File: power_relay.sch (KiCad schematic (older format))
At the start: 35 parts, among them J18 Conn_01x03, J20 Conn_01x03, J22 Conn_01x03, J24 Conn_01x03, J26 Conn_01x03, K1 RELAY_1RT, K2 RELAY_1RT, K3 RELAY_1RT, K4 RELAY_1RT, K5 RELAY_1RT, Q1 MMBT4401-7-F, Q10 SI7113ADN-T1-GE3, Q2 MMBT4401-7-F, Q3 MMBT4401-7-F, Q4 SI7113ADN-T1-GE3, Q5 SI7113ADN-T1-GE3, Q6 SI7113ADN-T1-GE3, Q7 MMBT4401-7-F, Q8 MMBT4401-7-F, Q9 SI7113ADN-T1-GE3

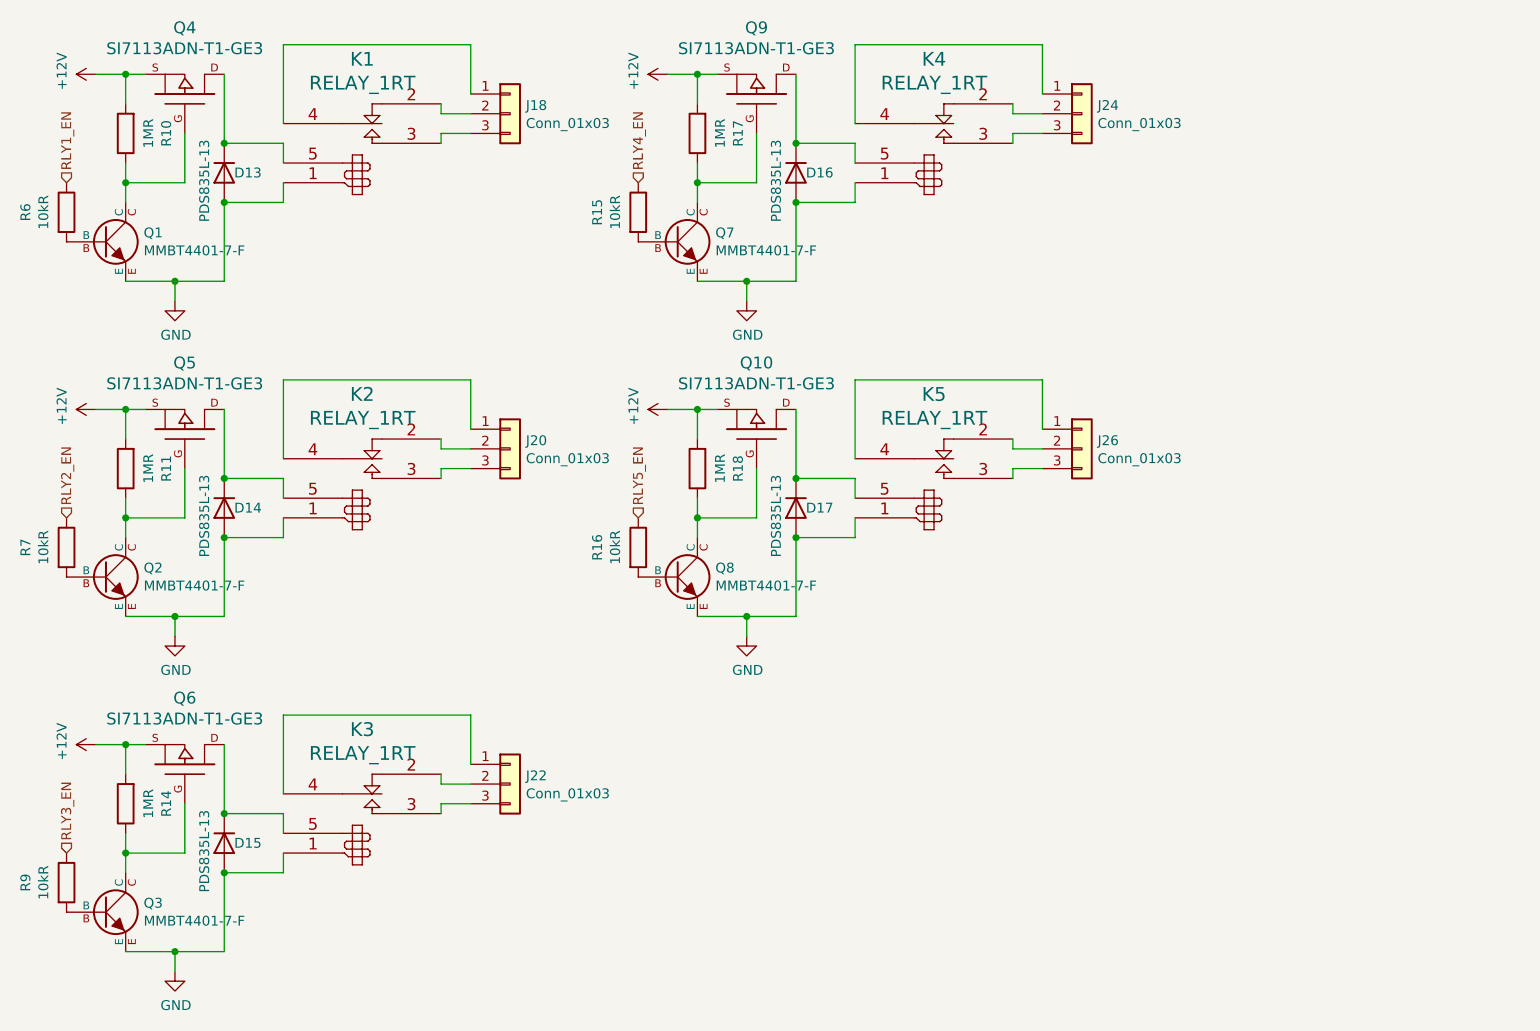
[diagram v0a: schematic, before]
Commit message: Positioning finished
Lacks fine alignment.
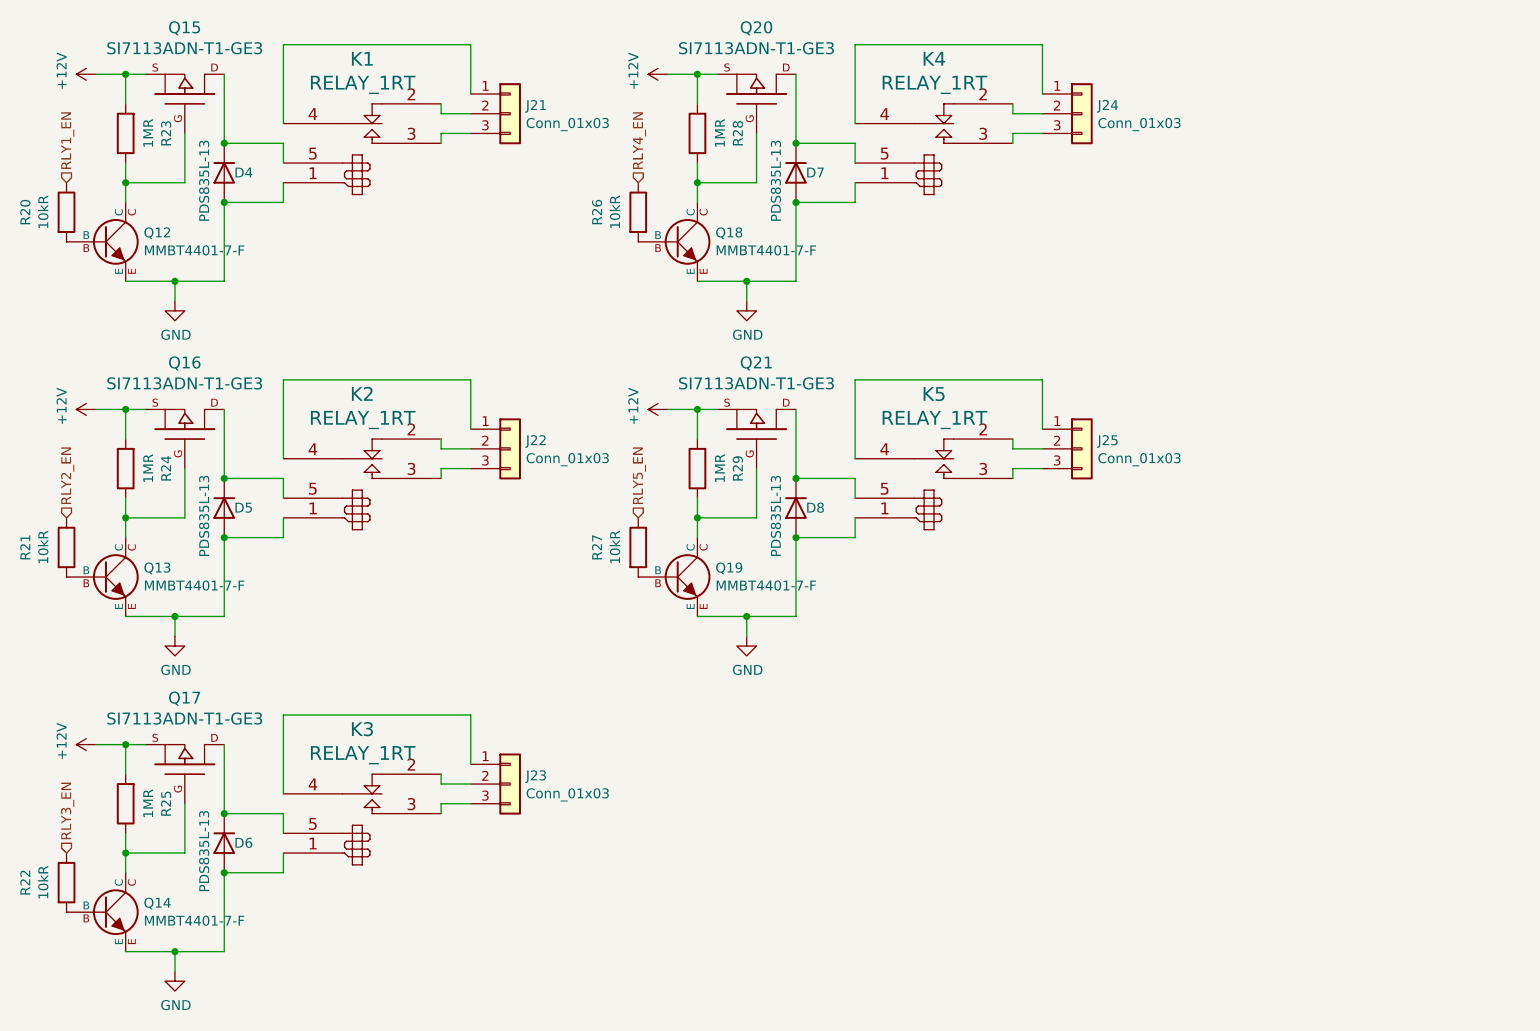
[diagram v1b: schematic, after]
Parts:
- renumbered D13 to D4, D14 to D5, D15 to D6, D16 to D7, D17 to D8, J18 to J21, J20 to J22, J22 to J23, J26 to J25, Q1 to Q12, Q2 to Q13, Q3 to Q14, Q4 to Q15, Q5 to Q16, Q6 to Q17, Q7 to Q18, Q8 to Q19, Q9 to Q20, Q10 to Q21, R6 to R20, R7 to R21, R9 to R22, R10 to R23, R11 to R24, R14 to R25, R15 to R26, R16 to R27, R17 to R28, R18 to R29

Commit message: Start MCU layout
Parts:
- renumbered J21 to J22, J22 to J23, J23 to J24, J24 to J25, J25 to J26
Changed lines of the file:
@@
 AR Path="/5E1C04CF/5E48FA57" Ref="#PWR?"  Part="1"
 AR Path="/5E3E0C4B/5E48FA57" Ref="#PWR?"  Part="1"
-AR Path="/5E4850C0/5E48FA57" Ref="#PWR055"  Part="1"
-F 0 "#PWR055" H 4050 2550 50  0001 C CNN
+AR Path="/5E4850C0/5E48FA57" Ref="#PWR059"  Part="1"
+F 0 "#PWR059" H 4050 2550 50  0001 C CNN
 F 1 "+12V" H 4065 2873 50  0000 C CNN
 F 2 "" H 4050 2700 50  0001 C CNN
@@
 AR Path="/5E1C04CF/5E48FA5D" Ref="#PWR?"  Part="1"
 AR Path="/5E3E0C4B/5E48FA5D" Ref="#PWR?"  Part="1"
-AR Path="/5E4850C0/5E48FA5D" Ref="#PWR057"  Part="1"
-F 0 "#PWR057" H 4450 3600 50  0001 C CNN
+AR Path="/5E4850C0/5E48FA5D" Ref="#PWR061"  Part="1"
+F 0 "#PWR061" H 4450 3600 50  0001 C CNN
 F 1 "GND" H 4455 3677 50  0000 C CNN
 F 2 "" H 4450 3850 50  0001 C CNN
@@
 P 6150 2900
 AR Path="/5E1C04CF/5E48FA71" Ref="J?"  Part="1"
-AR Path="/5E4850C0/5E48FA71" Ref="J25"  Part="1"
-F 0 "J25" H 6230 2942 50  0000 L CNN
+AR Path="/5E4850C0/5E48FA71" Ref="J26"  Part="1"
+F 0 "J26" H 6230 2942 50  0000 L CNN
 F 1 "Conn_01x03" H 6230 2851 50  0000 L CNN
 F 2 "TerminalBlock_Phoenix:TerminalBlock_Phoenix_PT-1,5-3-3.5-H_1x03_P3.50mm_Horizontal" H 6150 2900 50  0001 C CNN
@@
 AR Path="/5E1C04CF/5E48FAAF" Ref="#PWR?"  Part="1"
 AR Path="/5E3E0C4B/5E48FAAF" Ref="#PWR?"  Part="1"
-AR Path="/5E4850C0/5E48FAAF" Ref="#PWR054"  Part="1"
-F 0 "#PWR054" H 4050 850 50  0001 C CNN
+AR Path="/5E4850C0/5E48FAAF" Ref="#PWR058"  Part="1"
+F 0 "#PWR058" H 4050 850 50  0001 C CNN
 F 1 "+12V" H 4065 1173 50  0000 C CNN
 F 2 "" H 4050 1000 50  0001 C CNN
@@
 AR Path="/5E1C04CF/5E48FAB5" Ref="#PWR?"  Part="1"
 AR Path="/5E3E0C4B/5E48FAB5" Ref="#PWR?"  Part="1"
-AR Path="/5E4850C0/5E48FAB5" Ref="#PWR056"  Part="1"
-F 0 "#PWR056" H 4450 1900 50  0001 C CNN
+AR Path="/5E4850C0/5E48FAB5" Ref="#PWR060"  Part="1"
+F 0 "#PWR060" H 4450 1900 50  0001 C CNN
 F 1 "GND" H 4455 1977 50  0000 C CNN
 F 2 "" H 4450 2150 50  0001 C CNN
@@
 P 6150 1200
 AR Path="/5E1C04CF/5E48FAC9" Ref="J?"  Part="1"
-AR Path="/5E4850C0/5E48FAC9" Ref="J24"  Part="1"
-F 0 "J24" H 6230 1242 50  0000 L CNN
+AR Path="/5E4850C0/5E48FAC9" Ref="J25"  Part="1"
+F 0 "J25" H 6230 1242 50  0000 L CNN
 F 1 "Conn_01x03" H 6230 1151 50  0000 L CNN
 F 2 "TerminalBlock_Phoenix:TerminalBlock_Phoenix_PT-1,5-3-3.5-H_1x03_P3.50mm_Horizontal" H 6150 1200 50  0001 C CNN
@@
 AR Path="/5E1C04CF/5E48FB07" Ref="#PWR?"  Part="1"
 AR Path="/5E3E0C4B/5E48FB07" Ref="#PWR?"  Part="1"
-AR Path="/5E4850C0/5E48FB07" Ref="#PWR049"  Part="1"
-F 0 "#PWR049" H 1150 2550 50  0001 C CNN
+AR Path="/5E4850C0/5E48FB07" Ref="#PWR053"  Part="1"
+F 0 "#PWR053" H 1150 2550 50  0001 C CNN
 F 1 "+12V" H 1165 2873 50  0000 C CNN
 F 2 "" H 1150 2700 50  0001 C CNN
@@
 AR Path="/5E1C04CF/5E48FB0D" Ref="#PWR?"  Part="1"
 AR Path="/5E3E0C4B/5E48FB0D" Ref="#PWR?"  Part="1"
-AR Path="/5E4850C0/5E48FB0D" Ref="#PWR052"  Part="1"
-F 0 "#PWR052" H 1550 3600 50  0001 C CNN
+AR Path="/5E4850C0/5E48FB0D" Ref="#PWR056"  Part="1"
+F 0 "#PWR056" H 1550 3600 50  0001 C CNN
 F 1 "GND" H 1555 3677 50  0000 C CNN
 F 2 "" H 1550 3850 50  0001 C CNN
@@
 P 3250 2900
 AR Path="/5E1C04CF/5E48FB1A" Ref="J?"  Part="1"
-AR Path="/5E4850C0/5E48FB1A" Ref="J22"  Part="1"
-F 0 "J22" H 3330 2942 50  0000 L CNN
+AR Path="/5E4850C0/5E48FB1A" Ref="J23"  Part="1"
+F 0 "J23" H 3330 2942 50  0000 L CNN
 F 1 "Conn_01x03" H 3330 2851 50  0000 L CNN
 F 2 "TerminalBlock_Phoenix:TerminalBlock_Phoenix_PT-1,5-3-3.5-H_1x03_P3.50mm_Horizontal" H 3250 2900 50  0001 C CNN
@@
 AR Path="/5E1C04CF/5E48FB58" Ref="#PWR?"  Part="1"
 AR Path="/5E3E0C4B/5E48FB58" Ref="#PWR?"  Part="1"
-AR Path="/5E4850C0/5E48FB58" Ref="#PWR048"  Part="1"
-F 0 "#PWR048" H 1150 850 50  0001 C CNN
+AR Path="/5E4850C0/5E48FB58" Ref="#PWR052"  Part="1"
+F 0 "#PWR052" H 1150 850 50  0001 C CNN
 F 1 "+12V" H 1165 1173 50  0000 C CNN
 F 2 "" H 1150 1000 50  0001 C CNN
@@
 AR Path="/5E1C04CF/5E48FB5E" Ref="#PWR?"  Part="1"
 AR Path="/5E3E0C4B/5E48FB5E" Ref="#PWR?"  Part="1"
-AR Path="/5E4850C0/5E48FB5E" Ref="#PWR051"  Part="1"
-F 0 "#PWR051" H 1550 1900 50  0001 C CNN
+AR Path="/5E4850C0/5E48FB5E" Ref="#PWR055"  Part="1"
+F 0 "#PWR055" H 1550 1900 50  0001 C CNN
 F 1 "GND" H 1555 1977 50  0000 C CNN
 F 2 "" H 1550 2150 50  0001 C CNN
@@
 P 3250 1200
 AR Path="/5E1C04CF/5E48FB72" Ref="J?"  Part="1"
-AR Path="/5E4850C0/5E48FB72" Ref="J21"  Part="1"
-F 0 "J21" H 3330 1242 50  0000 L CNN
+AR Path="/5E4850C0/5E48FB72" Ref="J22"  Part="1"
+F 0 "J22" H 3330 1242 50  0000 L CNN
 F 1 "Conn_01x03" H 3330 1151 50  0000 L CNN
 F 2 "TerminalBlock_Phoenix:TerminalBlock_Phoenix_PT-1,5-3-3.5-H_1x03_P3.50mm_Horizontal" H 3250 1200 50  0001 C CNN
@@
 AR Path="/5E1C04CF/5E48FBB0" Ref="#PWR?"  Part="1"
 AR Path="/5E3E0C4B/5E48FBB0" Ref="#PWR?"  Part="1"
-AR Path="/5E4850C0/5E48FBB0" Ref="#PWR050"  Part="1"
-F 0 "#PWR050" H 1150 4250 50  0001 C CNN
+AR Path="/5E4850C0/5E48FBB0" Ref="#PWR054"  Part="1"
+F 0 "#PWR054" H 1150 4250 50  0001 C CNN
 F 1 "+12V" H 1165 4573 50  0000 C CNN
 F 2 "" H 1150 4400 50  0001 C CNN
@@
 AR Path="/5E1C04CF/5E48FBB6" Ref="#PWR?"  Part="1"
 AR Path="/5E3E0C4B/5E48FBB6" Ref="#PWR?"  Part="1"
-AR Path="/5E4850C0/5E48FBB6" Ref="#PWR053"  Part="1"
-F 0 "#PWR053" H 1550 5300 50  0001 C CNN
+AR Path="/5E4850C0/5E48FBB6" Ref="#PWR057"  Part="1"
+F 0 "#PWR057" H 1550 5300 50  0001 C CNN
 F 1 "GND" H 1555 5377 50  0000 C CNN
 F 2 "" H 1550 5550 50  0001 C CNN
@@
 P 3250 4600
 AR Path="/5E1C04CF/5E48FBCA" Ref="J?"  Part="1"
-AR Path="/5E4850C0/5E48FBCA" Ref="J23"  Part="1"
-F 0 "J23" H 3330 4642 50  0000 L CNN
+AR Path="/5E4850C0/5E48FBCA" Ref="J24"  Part="1"
+F 0 "J24" H 3330 4642 50  0000 L CNN
 F 1 "Conn_01x03" H 3330 4551 50  0000 L CNN
 F 2 "TerminalBlock_Phoenix:TerminalBlock_Phoenix_PT-1,5-3-3.5-H_1x03_P3.50mm_Horizontal" H 3250 4600 50  0001 C CNN

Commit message: Stash
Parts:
- renumbered J22 to J21, J23 to J22, J24 to J23, J25 to J24, J26 to J25
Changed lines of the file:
@@
 P 6150 2900
 AR Path="/5E1C04CF/5E48FA71" Ref="J?"  Part="1"
-AR Path="/5E4850C0/5E48FA71" Ref="J26"  Part="1"
-F 0 "J26" H 6230 2942 50  0000 L CNN
+AR Path="/5E4850C0/5E48FA71" Ref="J25"  Part="1"
+F 0 "J25" H 6230 2942 50  0000 L CNN
 F 1 "Conn_01x03" H 6230 2851 50  0000 L CNN
 F 2 "TerminalBlock_Phoenix:TerminalBlock_Phoenix_PT-1,5-3-3.5-H_1x03_P3.50mm_Horizontal" H 6150 2900 50  0001 C CNN
@@
 P 6150 1200
 AR Path="/5E1C04CF/5E48FAC9" Ref="J?"  Part="1"
-AR Path="/5E4850C0/5E48FAC9" Ref="J25"  Part="1"
-F 0 "J25" H 6230 1242 50  0000 L CNN
+AR Path="/5E4850C0/5E48FAC9" Ref="J24"  Part="1"
+F 0 "J24" H 6230 1242 50  0000 L CNN
 F 1 "Conn_01x03" H 6230 1151 50  0000 L CNN
 F 2 "TerminalBlock_Phoenix:TerminalBlock_Phoenix_PT-1,5-3-3.5-H_1x03_P3.50mm_Horizontal" H 6150 1200 50  0001 C CNN
@@
 P 3250 2900
 AR Path="/5E1C04CF/5E48FB1A" Ref="J?"  Part="1"
-AR Path="/5E4850C0/5E48FB1A" Ref="J23"  Part="1"
-F 0 "J23" H 3330 2942 50  0000 L CNN
+AR Path="/5E4850C0/5E48FB1A" Ref="J22"  Part="1"
+F 0 "J22" H 3330 2942 50  0000 L CNN
 F 1 "Conn_01x03" H 3330 2851 50  0000 L CNN
 F 2 "TerminalBlock_Phoenix:TerminalBlock_Phoenix_PT-1,5-3-3.5-H_1x03_P3.50mm_Horizontal" H 3250 2900 50  0001 C CNN
@@
 P 3250 1200
 AR Path="/5E1C04CF/5E48FB72" Ref="J?"  Part="1"
-AR Path="/5E4850C0/5E48FB72" Ref="J22"  Part="1"
-F 0 "J22" H 3330 1242 50  0000 L CNN
+AR Path="/5E4850C0/5E48FB72" Ref="J21"  Part="1"
+F 0 "J21" H 3330 1242 50  0000 L CNN
 F 1 "Conn_01x03" H 3330 1151 50  0000 L CNN
 F 2 "TerminalBlock_Phoenix:TerminalBlock_Phoenix_PT-1,5-3-3.5-H_1x03_P3.50mm_Horizontal" H 3250 1200 50  0001 C CNN
@@
 P 3250 4600
 AR Path="/5E1C04CF/5E48FBCA" Ref="J?"  Part="1"
-AR Path="/5E4850C0/5E48FBCA" Ref="J24"  Part="1"
-F 0 "J24" H 3330 4642 50  0000 L CNN
+AR Path="/5E4850C0/5E48FBCA" Ref="J23"  Part="1"
+F 0 "J23" H 3330 4642 50  0000 L CNN
 F 1 "Conn_01x03" H 3330 4551 50  0000 L CNN
 F 2 "TerminalBlock_Phoenix:TerminalBlock_Phoenix_PT-1,5-3-3.5-H_1x03_P3.50mm_Horizontal" H 3250 4600 50  0001 C CNN
